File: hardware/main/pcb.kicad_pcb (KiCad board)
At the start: 2 copper layers, 55 x 55 mm, 29 parts, among them J3 Conn_01x03_Socket, Q1 BC547, Q2 BC547, Q3 BC547

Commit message: update the pcb
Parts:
- added J1: Conn_01x02_Socket, Connector_PinSocket_2.54mm:PinSocket_2x01_P2.54mm_Vertical, F.Cu at (140.2, 87.5)
- U1: value ~ -> ESP32 C3 supper mini
- moved J3 0.48 mm to (136.6, 87.6)
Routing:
- net +5V: track 66.6 -> 70.4 mm
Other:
- board text added: "SIGNAL"
- board text removed: "SUCCESS"

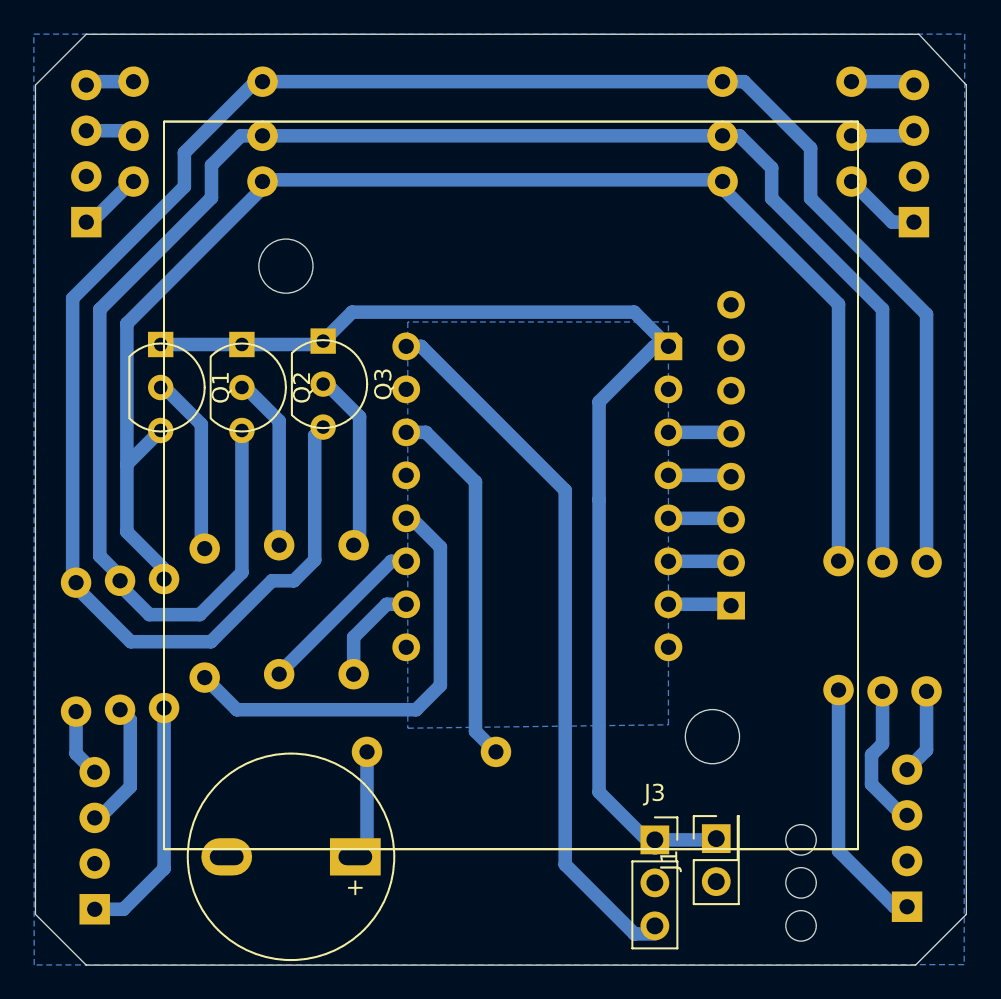
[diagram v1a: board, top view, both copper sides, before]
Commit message: Simplify device (#46)
* add tag emular tool

* fix the buzzer

* make board ready for 1.0.0-alfa1

* remove the error pin

* update the firmware tests

* update git ignore
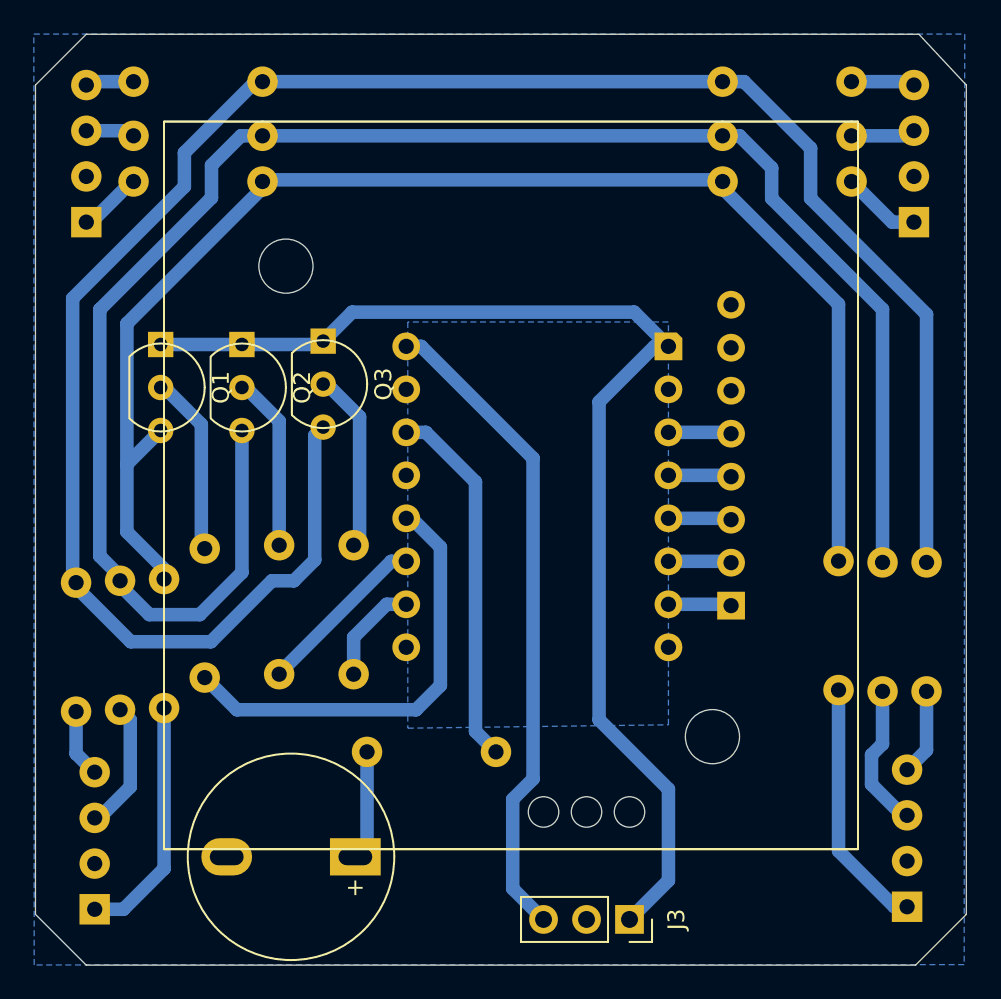
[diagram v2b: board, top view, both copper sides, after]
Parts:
- removed J1: Conn_01x02_Socket, Connector_PinSocket_2.54mm:PinSocket_2x01_P2.54mm_Vertical
- moved J3 4.93 mm to (135.1, 92.3), turned to -90 degrees
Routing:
- net Net-(J3-Pin_3): track 42.3 -> 39.1 mm
